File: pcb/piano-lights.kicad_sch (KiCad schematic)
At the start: 38 parts, among them J1 FTDI RS232, J2 USB-C 6-Pin, J3 LED Strip, J4 AVR-ISP-6, J5 MIDI IN, J6 MIDI THRU, J7 MIDI Coupler Out, J8 MIDI Coupler In, SW1 Button, SW2 Reset, U1 ATmega328, U2 H11L1, U3 74AHC1G125, Y1 16MHz

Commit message: Minre schematic tweaks
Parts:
- J7: value MIDI Coupler Out -> MIDI Coupler B
- J8: value MIDI Coupler In -> MIDI Coupler A
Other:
- note added: "USB-C Power"
- note removed: "USB Power"
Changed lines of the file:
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@@
     (stroke (width 0) (type default) (color 0 0 0 0))
   )
-  (polyline (pts (xy 50.8 178.054) (xy 50.8 160.274))
+  (polyline (pts (xy 48.26 179.07) (xy 48.26 161.29))
     (stroke (width 0) (type default) (color 0 0 0 0))
   )
@@
     (stroke (width 0) (type default) (color 0 0 0 0))
   )
-  (polyline (pts (xy 25.4 160.274) (xy 25.4 178.054))
+  (polyline (pts (xy 25.4 161.29) (xy 25.4 179.07))
     (stroke (width 0) (type default) (color 0 0 0 0))
   )
@@
     (stroke (width 0) (type default) (color 0 0 0 0))
   )
-  (wire (pts (xy 33.02 167.894) (xy 33.02 172.974))
+  (wire (pts (xy 31.75 167.64) (xy 31.75 172.72))
     (stroke (width 0) (type default) (color 0 0 0 0))
   )
@@
     (stroke (width 0) (type default) (color 0 0 0 0))
   )
-  (polyline (pts (xy 25.4 160.274) (xy 50.8 160.274))
+  (polyline (pts (xy 25.4 161.29) (xy 48.26 161.29))
     (stroke (width 0) (type default) (color 0 0 0 0))
   )
@@
     (stroke (width 0) (type default) (color 0 0 0 0))
   )
-  (wire (pts (xy 43.18 167.894) (xy 43.18 172.974))
+  (wire (pts (xy 41.91 167.64) (xy 41.91 172.72))
     (stroke (width 0) (type default) (color 0 0 0 0))
   )
@@
     (stroke (width 0) (type default) (color 0 0 0 0))
   )
-  (polyline (pts (xy 25.4 178.054) (xy 50.8 178.054))
+  (polyline (pts (xy 25.4 179.07) (xy 48.26 179.07))
     (stroke (width 0) (type default) (color 0 0 0 0))
   )
@@
     (effects (font (size 1.27 1.27)) (justify left bottom))
   )
-  (text "USB Power" (at 36.195 63.5 0)
+  (text "USB-C Power" (at 35.56 63.5 0)
     (effects (font (size 2.54 2.54) (thickness 0.508) bold italic) (justify left bottom))
   )
@@
     (effects (font (size 2.54 2.54) (thickness 0.508) bold italic) (justify left bottom))
   )
-  (text "Power Flags" (at 25.4 159.766 0)
-    (effects (font (size 1.27 1.27)) (justify left bottom))
-  )
-  (text "M3 Mounting Holes" (at 25.4 183.515 0)
+  (text "Power Flags" (at 25.4 160.02 0)
+    (effects (font (size 1.27 1.27)) (justify left bottom))
+  )
+  (text "M3 Mounting Holes" (at 25.4 182.88 0)
     (effects (font (size 1.27 1.27)) (justify left bottom))
   )
@@
     (pin "1")
   )
-  (symbol (lib_id "power:PWR_FLAG") (at 43.18 167.894 0) (unit 1)
-    (in_bom yes) (on_board yes)
-    (property "Reference" "#FLG01" (id 0) (at 43.18 165.989 0)
-      (effects (font (size 1.27 1.27)) hide)
-    )
-    (property "Value" "PWR_FLAG" (id 1) (at 43.18 164.084 0))
-    (property "Footprint" "" (id 2) (at 43.18 167.894 0)
-      (effects (font (size 1.27 1.27)) hide)
-    )
-    (property "Datasheet" "~" (id 3) (at 43.18 167.894 0)
+  (symbol (lib_id "power:PWR_FLAG") (at 41.91 167.64 0) (unit 1)
+    (in_bom yes) (on_board yes)
+    (property "Reference" "#FLG01" (id 0) (at 41.91 165.735 0)
+      (effects (font (size 1.27 1.27)) hide)
+    )
+    (property "Value" "PWR_FLAG" (id 1) (at 41.91 163.83 0))
+    (property "Footprint" "" (id 2) (at 41.91 167.64 0)
+      (effects (font (size 1.27 1.27)) hide)
+    )
+    (property "Datasheet" "~" (id 3) (at 41.91 167.64 0)
       (effects (font (size 1.27 1.27)) hide)
     )
@@
     (pin "1")
   )
-  (symbol (lib_id "power:GND") (at 43.18 172.974 0) (unit 1)
+  (symbol (lib_id "power:GND") (at 41.91 172.72 0) (unit 1)
     (in_bom yes) (on_board yes) (fields_autoplaced)
-    (property "Reference" "#PWR032" (id 0) (at 43.18 179.324 0)
-      (effects (font (size 1.27 1.27)) hide)
-    )
-    (property "Value" "GND" (id 1) (at 43.18 178.054 0)
-      (effects (font (size 1.27 1.27)) hide)
-    )
-    (property "Footprint" "" (id 2) (at 43.18 172.974 0)
-      (effects (font (size 1.27 1.27)) hide)
-    )
-    (property "Datasheet" "" (id 3) (at 43.18 172.974 0)
+    (property "Reference" "#PWR032" (id 0) (at 41.91 179.07 0)
+      (effects (font (size 1.27 1.27)) hide)
+    )
+    (property "Value" "GND" (id 1) (at 41.91 177.8 0)
+      (effects (font (size 1.27 1.27)) hide)
+    )
+    (property "Footprint" "" (id 2) (at 41.91 172.72 0)
+      (effects (font (size 1.27 1.27)) hide)
+    )
+    (property "Datasheet" "" (id 3) (at 41.91 172.72 0)
       (effects (font (size 1.27 1.27)) hide)
     )
@@
     (in_bom yes) (on_board yes)
     (property "Reference" "U1" (id 0) (at 127 36.83 0))
-    (property "Value" "ATmega328" (id 1) (at 125.73 110.49 0))
+    (property "Value" "ATmega328" (id 1) (at 123.19 110.49 0))
     (property "Footprint" "Package_QFP:TQFP-32_7x7mm_P0.8mm" (id 2) (at 96.52 68.58 0)
       (effects (font (size 1.27 1.27) italic) hide)
@@
     )
   )
-  (symbol (lib_id "power:PWR_FLAG") (at 33.02 172.974 180) (unit 1)
-    (in_bom yes) (on_board yes)
-    (property "Reference" "#FLG02" (id 0) (at 33.02 174.879 0)
-      (effects (font (size 1.27 1.27)) hide)
-    )
-    (property "Value" "PWR_FLAG" (id 1) (at 33.02 176.784 0))
-    (property "Footprint" "" (id 2) (at 33.02 172.974 0)
-      (effects (font (size 1.27 1.27)) hide)
-    )
-    (property "Datasheet" "~" (id 3) (at 33.02 172.974 0)
+  (symbol (lib_id "power:PWR_FLAG") (at 31.75 172.72 180) (unit 1)
+    (in_bom yes) (on_board yes)
+    (property "Reference" "#FLG02" (id 0) (at 31.75 174.625 0)
+      (effects (font (size 1.27 1.27)) hide)
+    )
+    (property "Value" "PWR_FLAG" (id 1) (at 31.75 176.53 0))
+    (property "Footprint" "" (id 2) (at 31.75 172.72 0)
+      (effects (font (size 1.27 1.27)) hide)
+    )
+    (property "Datasheet" "~" (id 3) (at 31.75 172.72 0)
       (effects (font (size 1.27 1.27)) hide)
     )
@@
     (pin "SH")
   )
-  (symbol (lib_id "power:+5V") (at 33.02 167.894 0) (mirror y) (unit 1)
-    (in_bom yes) (on_board yes)
-    (property "Reference" "#PWR031" (id 0) (at 33.02 171.704 0)
-      (effects (font (size 1.27 1.27)) hide)
-    )
-    (property "Value" "+5V" (id 1) (at 33.02 164.084 0))
-    (property "Footprint" "" (id 2) (at 33.02 167.894 0)
-      (effects (font (size 1.27 1.27)) hide)
-    )
-    (property "Datasheet" "" (id 3) (at 33.02 167.894 0)
+  (symbol (lib_id "power:+5V") (at 31.75 167.64 0) (mirror y) (unit 1)
+    (in_bom yes) (on_board yes)
+    (property "Reference" "#PWR031" (id 0) (at 31.75 171.45 0)
+      (effects (font (size 1.27 1.27)) hide)
+    )
+    (property "Value" "+5V" (id 1) (at 31.75 163.83 0))
+    (property "Footprint" "" (id 2) (at 31.75 167.64 0)
+      (effects (font (size 1.27 1.27)) hide)
+    )
+    (property "Datasheet" "" (id 3) (at 31.75 167.64 0)
       (effects (font (size 1.27 1.27)) hide)
     )
@@
       (effects (font (size 1.27 1.27)) (justify left))
     )
-    (property "Value" "MIDI Coupler In" (id 1) (at 205.74 138.43 0)
+    (property "Value" "MIDI Coupler A" (id 1) (at 205.74 138.43 0)
       (effects (font (size 1.27 1.27)) (justify left))
     )
@@
       (effects (font (size 1.27 1.27)) (justify left))
     )
-    (property "Value" "MIDI Coupler Out" (id 1) (at 228.6 137.922 0)
+    (property "Value" "MIDI Coupler B" (id 1) (at 228.6 137.922 0)
       (effects (font (size 1.27 1.27)) (justify left))
     )
@@
     )
     (path "/f9866f8b-3936-4706-bae6-722d71235ee8"
-      (reference "J7") (unit 1) (value "MIDI Coupler Out") (footprint "00-Vendor_SDS-50J:CUI_SDS-50J")
+      (reference "J7") (unit 1) (value "MIDI Coupler B") (footprint "00-Vendor_SDS-50J:CUI_SDS-50J")
     )
     (path "/c47e7649-31b9-489c-93da-965a4a52c822"
-      (reference "J8") (unit 1) (value "MIDI Coupler In") (footprint "00-Vendor_SDS-50J:CUI_SDS-50J")
+      (reference "J8") (unit 1) (value "MIDI Coupler A") (footprint "00-Vendor_SDS-50J:CUI_SDS-50J")
     )
     (path "/f3058dab-f2e9-49c6-8907-75a98c2494ef"

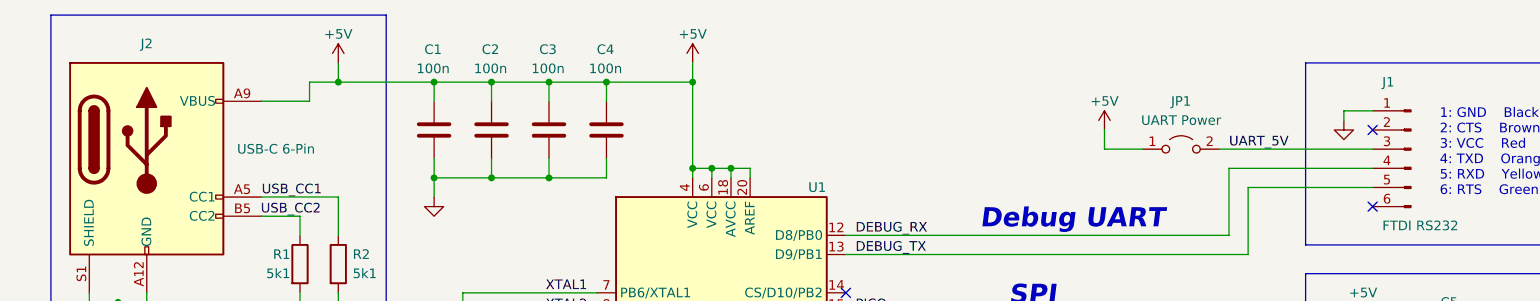
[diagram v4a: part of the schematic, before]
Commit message: Swap J1 and J2 designators so J1 is at the upper left
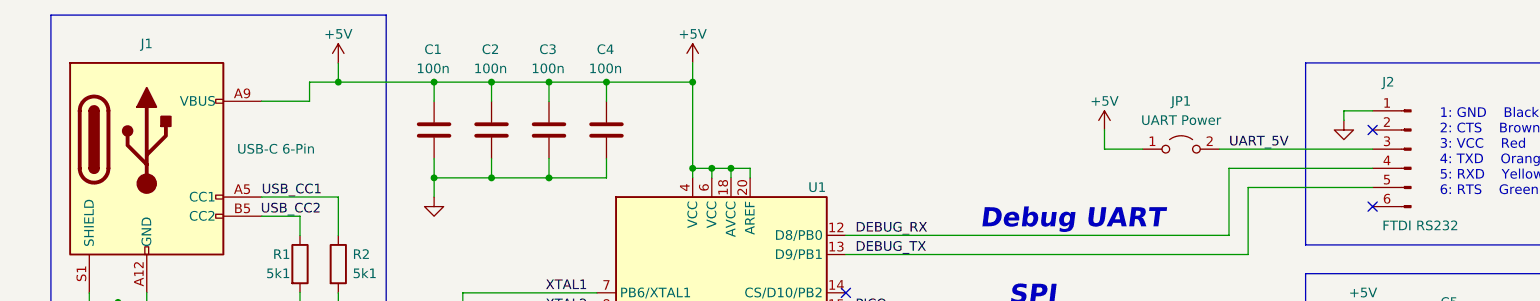
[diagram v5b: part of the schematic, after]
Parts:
- renumbered J2 to J1, J1 to J2
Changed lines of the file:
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@@
   (symbol (lib_id "Connector:Conn_01x06_Male") (at 205.74 31.75 0) (mirror y) (unit 1)
     (in_bom yes) (on_board yes)
-    (property "Reference" "J1" (id 0) (at 201.93 22.86 0)
+    (property "Reference" "J2" (id 0) (at 201.93 22.86 0)
       (effects (font (size 1.27 1.27)) (justify right))
     )
@@
   (symbol (lib_id "Connector:USB_C_Receptacle_PowerOnly_6P") (at 38.1 33.02 0) (unit 1)
     (in_bom yes) (on_board yes)
-    (property "Reference" "J2" (id 0) (at 38.1 17.78 0))
+    (property "Reference" "J1" (id 0) (at 38.1 17.78 0))
     (property "Value" "USB-C 6-Pin" (id 1) (at 55.245 31.75 0))
     (property "Footprint" "00-USB_C_GCT:GCT_USB4125-GF-A-0190_REVA2" (id 2) (at 41.91 30.48 0)
@@
       (reference "H4") (unit 1) (value "MountingHole") (footprint "MountingHole:MountingHole_3.2mm_M3")
     )
+    (path "/f7370afb-cec9-4b13-bff1-cf67a638138b"
+      (reference "J1") (unit 1) (value "USB-C 6-Pin") (footprint "00-USB_C_GCT:GCT_USB4125-GF-A-0190_REVA2")
+    )
     (path "/33bc4d7e-ec67-4ad9-8b68-988d7745711a"
-      (reference "J1") (unit 1) (value "FTDI RS232") (footprint "Connector_PinHeader_2.54mm:PinHeader_1x06_P2.54mm_Vertical")
-    )
-    (path "/f7370afb-cec9-4b13-bff1-cf67a638138b"
-      (reference "J2") (unit 1) (value "USB-C 6-Pin") (footprint "00-USB_C_GCT:GCT_USB4125-GF-A-0190_REVA2")
+      (reference "J2") (unit 1) (value "FTDI RS232") (footprint "Connector_PinHeader_2.54mm:PinHeader_1x06_P2.54mm_Vertical")
     )
     (path "/2c9565e8-406b-43f1-b981-325aa0f42208"

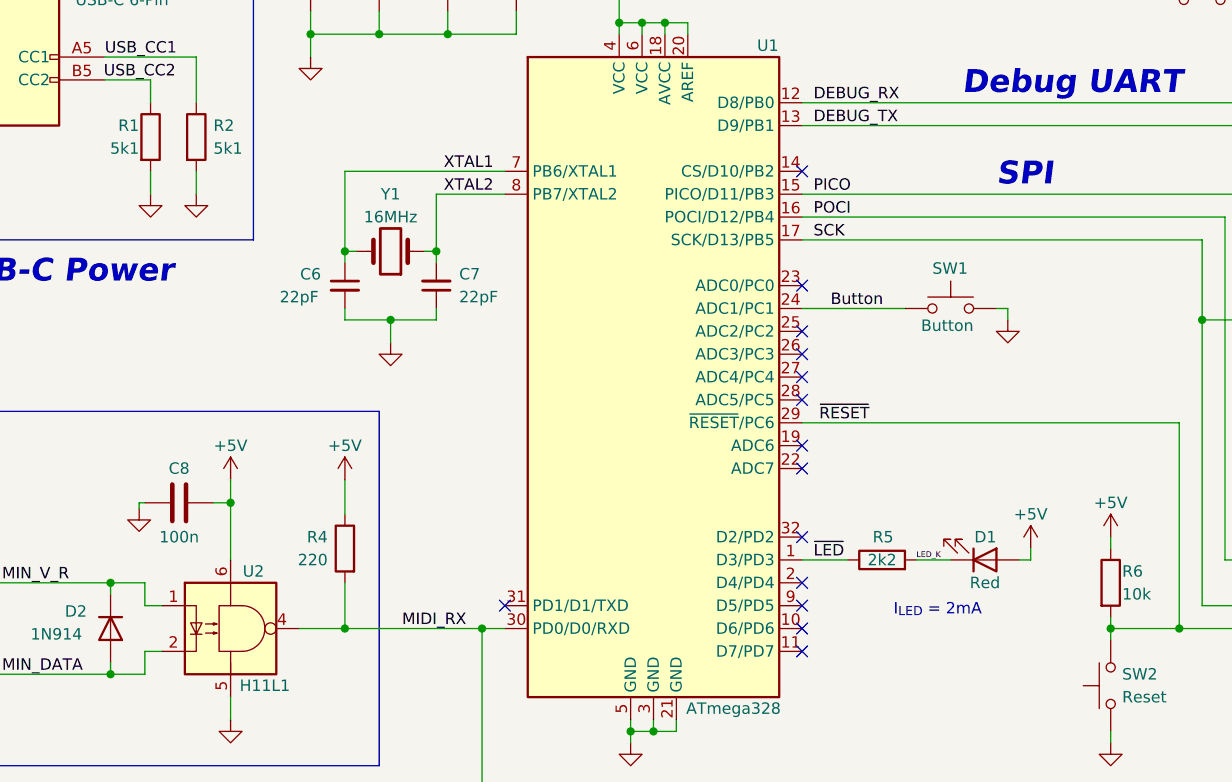
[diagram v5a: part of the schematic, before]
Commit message: Set Mfr, Mfr Part, and Vendor on most other components
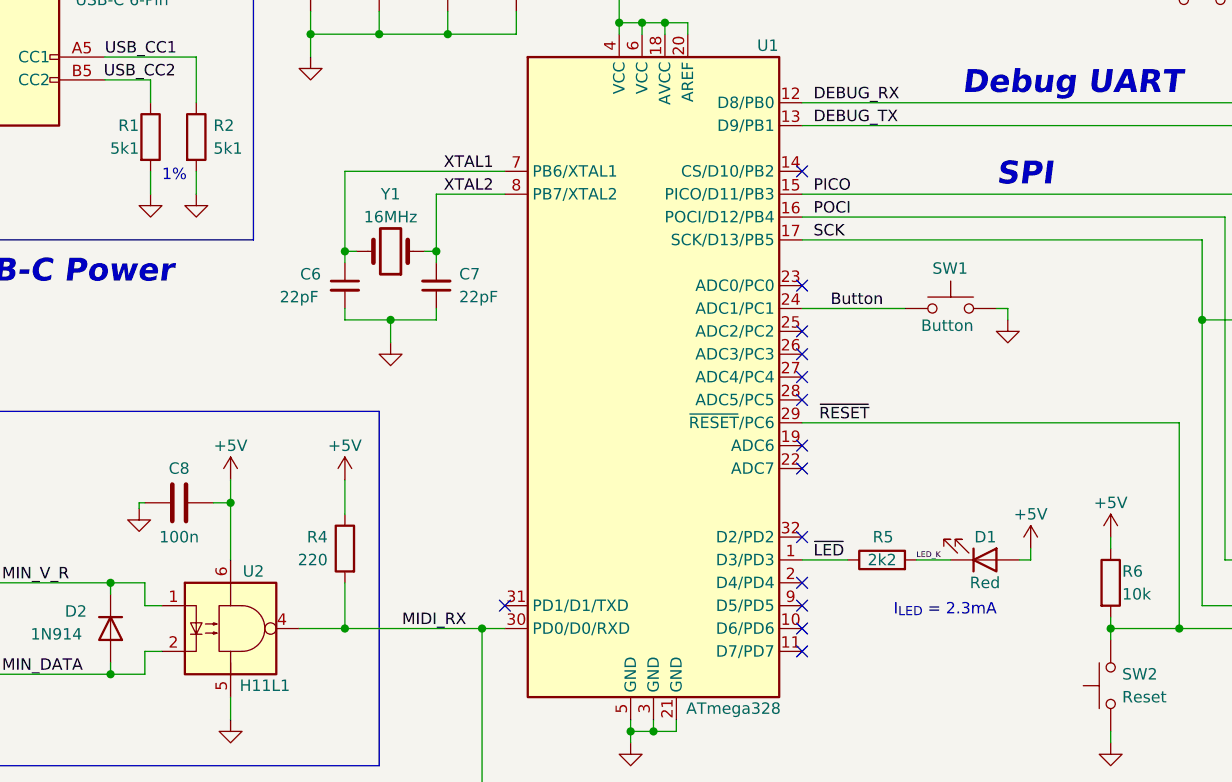
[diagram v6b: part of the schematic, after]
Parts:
- C1, C2, C3, C4, C8, C9: Mfr (none) -> Murata; Mfr Part (none) -> GRM188R72A104KA35D; Vendor (none) -> https://www.digikey.com/short/f338mhm4
- C6, C7: Mfr (none) -> Murata; Mfr Part (none) -> GCM1885C2A220JA16D; Vendor (none) -> https://www.digikey.com/short/njdjmrvt
- D1: Vendor https://www.digikey.com/en/products/detail/lumex-opto-compo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 -> https://www.digikey.com/short/pq7bjprd
- D2: Mfr (none) -> Microchip; Mfr Part (none) -> 1N4148UR-1; Vendor (none) -> https://www.digikey.com/short/hhwb3nh4
- J1: Mfr (none) -> GCT; Mfr Part (none) -> USB4125-GF-A-0190; Vendor (none) -> https://www.digikey.com/short/vczqh5b7
- J4: Vendor https://www.digikey.com/en/products/detail/metz-connect-usa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 -> https://www.digikey.com/short/hfmdj3qw
- J5: Vendor https://www.digikey.com/en/products/detail/cui-devices/SDS-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 -> https://www.digikey.com/short/qh7jzdb5
- J6, J7, J8: Mfr (none) -> CUI; Mrf CUI -> (none); Vendor https://www.digikey.com/en/products/detail/cui-devices/SDS-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 -> https://www.digikey.com/short/qh7jzdb5
- R1, R2: Mfr (none) -> Yageo; Mfr Part (none) -> RC0603FR-075K1L; Vendor (none) -> https://www.digikey.com/short/wbwf4hdv
- R3, R4, R7, R8: Mfr (none) -> Yageo; Mfr Part (none) -> RC0603JR-07220RL; Vendor (none) -> https://www.digikey.com/short/4h4r3cw4
- R5: Mfr (none) -> Yageo; Mfr Part (none) -> RC0603JR-072K2L; Vendor (none) -> https://www.digikey.com/short/d0045h9c
- R6: Mfr (none) -> Yageo; Mfr Part (none) -> RC0603JR-0710KL; Vendor (none) -> https://www.digikey.com/short/53r9v330
- SW1, SW2: Vendor https://www.digikey.com/en/products/detail/cit-relay-and-sw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 -> https://www.digikey.com/short/j102mwb0
- U1: Vendor https://www.digikey.com/en/products/detail/microchip-techno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 -> https://www.digikey.com/short/d1bvw084
- U2: Mfr (none) -> onsemi; Mrf onsemi -> (none); Vendor https://www.digikey.com/en/products/detail/onsemi/H11L1M/28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 -> https://www.digikey.com/short/bnt2r2pp
- U3: Vendor https://www.digikey.com/en/products/detail/nexperia-usa-inc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 -> https://www.digikey.com/short/289d5942
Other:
- note added: "1%"
- note added: "I_{LED} = 2.3mA"
- note removed: "I_{LED} = 2mA"
